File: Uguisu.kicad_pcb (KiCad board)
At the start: 2 copper layers, 35 x 50 mm, 8 parts, among them U1 XIAO-nRF52840-SMD

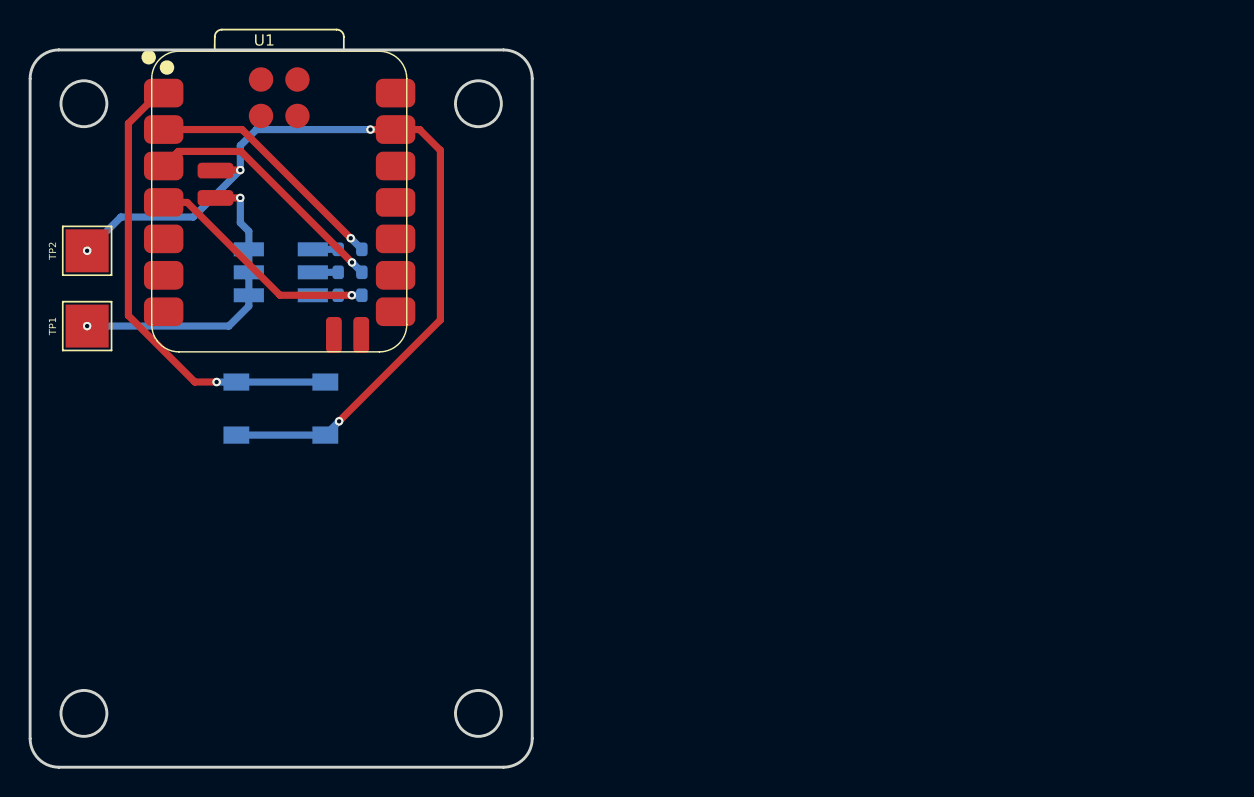
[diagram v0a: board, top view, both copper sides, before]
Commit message: hw: add 3.3V and GND test point pads for AirTag power tap
- Label U1 3V3 pin as /3.3V net (was unconnected)
- Add 3x3mm SMD test point pads for 3.3V and GND adjacent to XIAO
- Rename existing BATT/GND test points with clearer silkscreen labels
- Route 3.3V net to test point via back copper
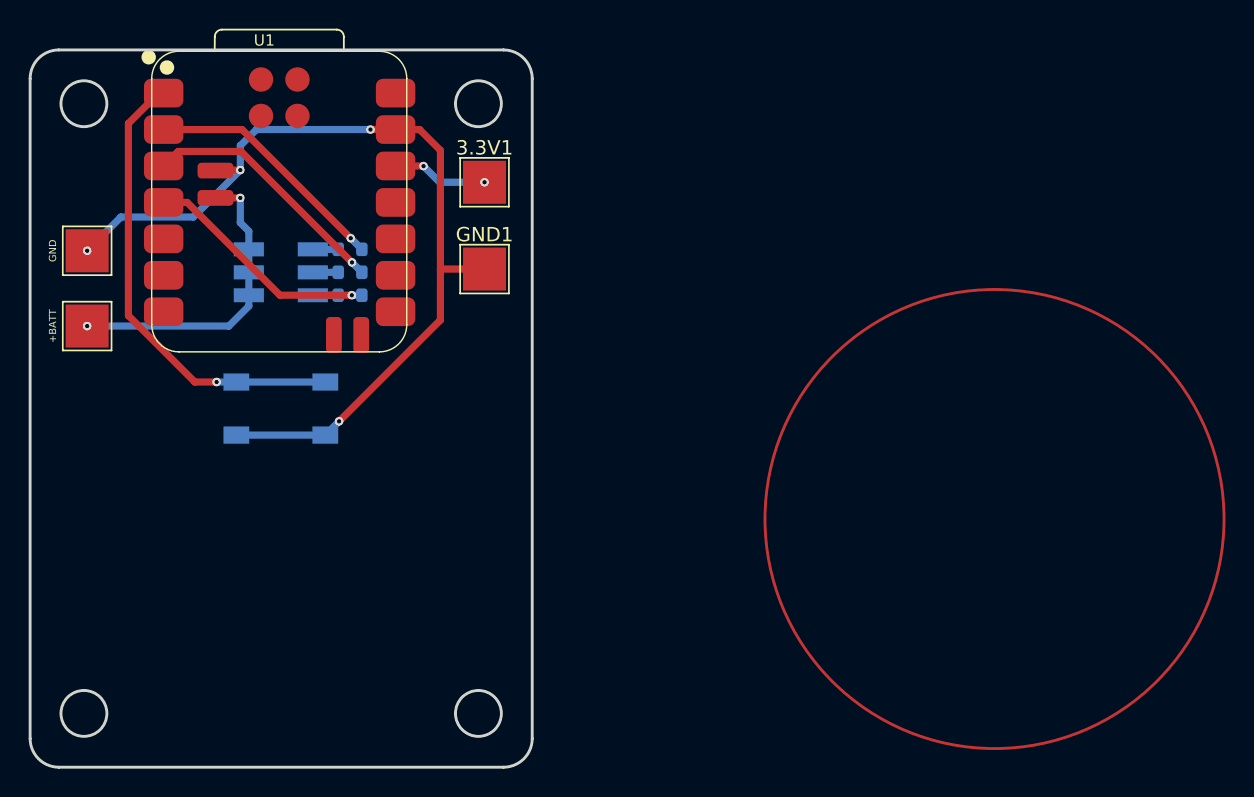
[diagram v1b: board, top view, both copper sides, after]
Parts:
- added 3.3V1: 3.3V, TestPoint:TestPoint_Pad_3.0x3.0mm, F.Cu at (133.2, 70.0)
- added GND1: GND, TestPoint:TestPoint_Pad_3.0x3.0mm, F.Cu at (133.2, 76.0)
- renumbered TP1 to +BATT, TP2 to GND
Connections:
- U1 pad 12: unconnected-(U1-3V3-Pad12) -> /3.3V
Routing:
- net /3.3V: track 0.00 -> 6.67 mm, vias 0 -> 2
- net GND: track 60.9 -> 64.0 mm
